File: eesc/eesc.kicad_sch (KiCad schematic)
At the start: 0 parts

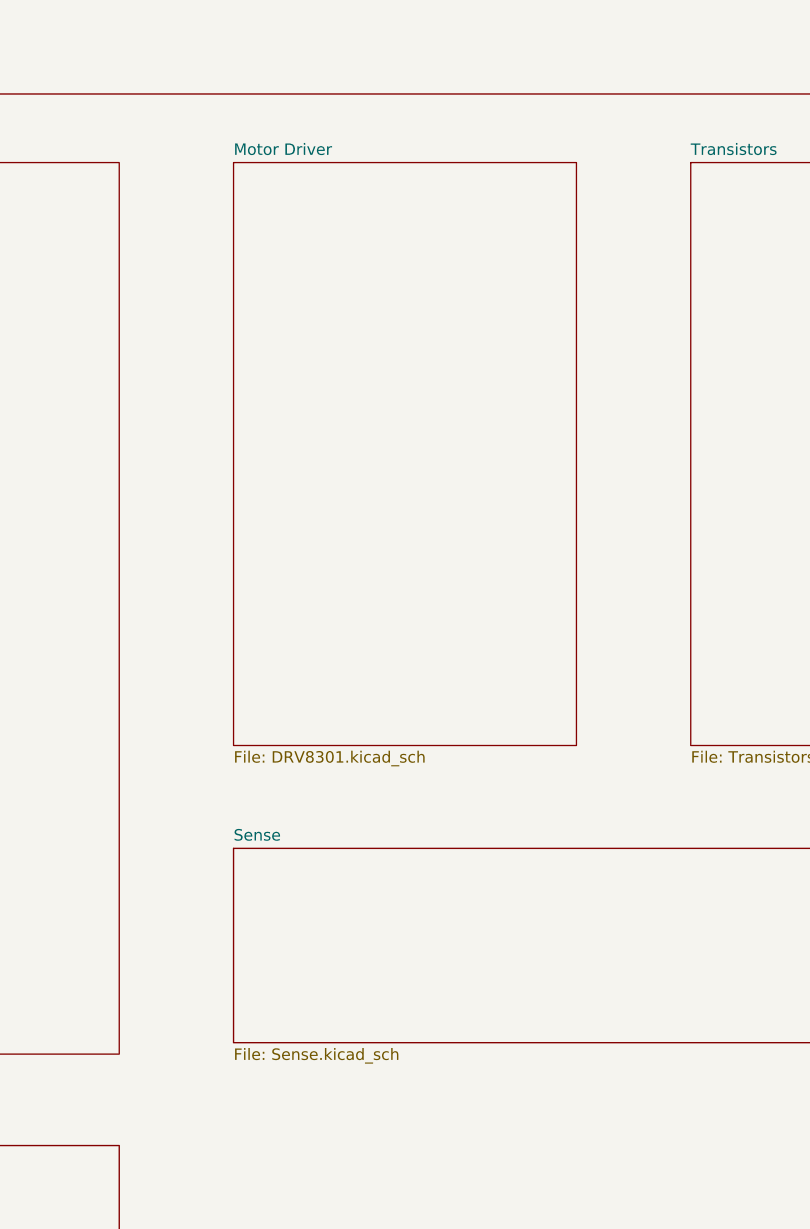
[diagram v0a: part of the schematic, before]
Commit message: Complete transistor stage
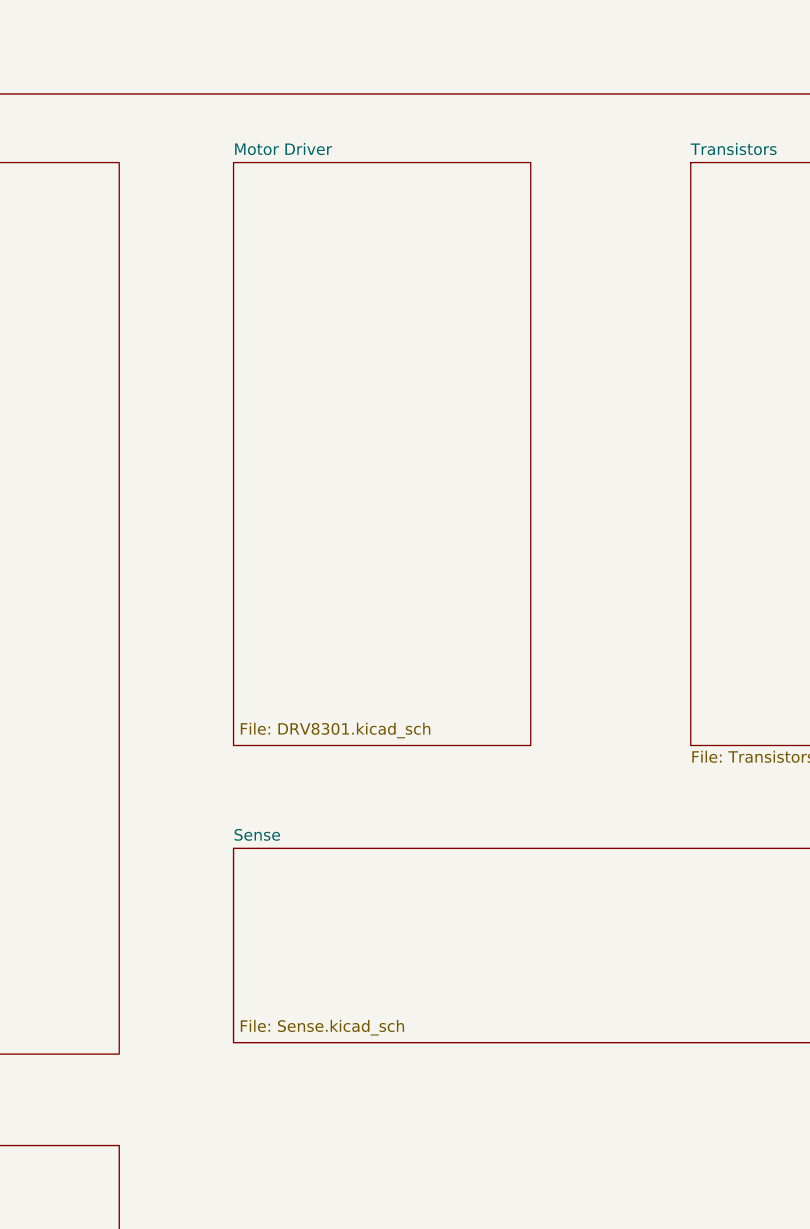
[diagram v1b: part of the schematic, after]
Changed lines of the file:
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@@
     )
   )
-  (sheet (at 177.8 44.45) (size 38.1 64.77) (fields_autoplaced)
+  (sheet (at 177.8 44.45) (size 33.02 64.77)
     (stroke (width 0.127) (type solid))
     (fill (color 0 0 0 0.0000))
@@
       (effects (font (size 1.27 1.27)) (justify left bottom))
     )
-    (property "Sheetfile" "DRV8301.kicad_sch" (at 177.8 109.7919 0)
+    (property "Sheetfile" "DRV8301.kicad_sch" (at 178.435 106.68 0)
       (effects (font (size 1.27 1.27)) (justify left top))
     )
@@
     )
   )
-  (sheet (at 177.8 120.65) (size 88.9 21.59) (fields_autoplaced)
+  (sheet (at 177.8 120.65) (size 88.9 21.59)
     (stroke (width 0.1524) (type solid))
     (fill (color 0 0 0 0.0000))
@@
       (effects (font (size 1.27 1.27)) (justify left bottom))
     )
-    (property "Sheetfile" "Sense.kicad_sch" (at 177.8 142.8246 0)
+    (property "Sheetfile" "Sense.kicad_sch" (at 178.435 139.7 0)
       (effects (font (size 1.27 1.27)) (justify left top))
     )

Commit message: Most updated changes
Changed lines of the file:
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@@
     )
   )
-  (sheet (at 228.6 44.45) (size 38.1 64.77) (fields_autoplaced)
+  (sheet (at 228.6 44.45) (size 38.1 64.135)
     (stroke (width 0.127) (type solid))
     (fill (color 0 0 0 0.0000))
@@
       (effects (font (size 1.27 1.27)) (justify left bottom))
     )
-    (property "Sheetfile" "Transistors.kicad_sch" (at 228.6 109.7919 0)
+    (property "Sheetfile" "Transistors.kicad_sch" (at 228.6 106.045 0)
       (effects (font (size 1.27 1.27)) (justify left top))
     )
@@
     )
   )
-  (sheet (at 54.61 114.3) (size 24.13 11.43) (fields_autoplaced)
+  (sheet (at 54.61 132.08) (size 24.13 11.43) (fields_autoplaced)
     (stroke (width 0.1524) (type solid))
     (fill (color 0 0 0 0.0000))
-    (property "Sheetname" "NRF" (at 54.61 113.5884 0)
+    (property "Sheetname" "NRF" (at 54.61 131.3684 0)
       (effects (font (size 1.27 1.27)) (justify left bottom))
     )
-    (property "Sheetfile" "NRF.kicad_sch" (at 54.61 126.3146 0)
+    (property "Sheetfile" "NRF.kicad_sch" (at 54.61 144.0946 0)
       (effects (font (size 1.27 1.27)) (justify left top))
     )
-    (property "Field2" "" (at 54.61 114.3 0)
+    (property "Field2" "" (at 54.61 132.08 0)
       (effects (font (size 1.27 1.27)) hide)
     )
